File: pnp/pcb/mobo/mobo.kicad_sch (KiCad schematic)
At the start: 0 parts

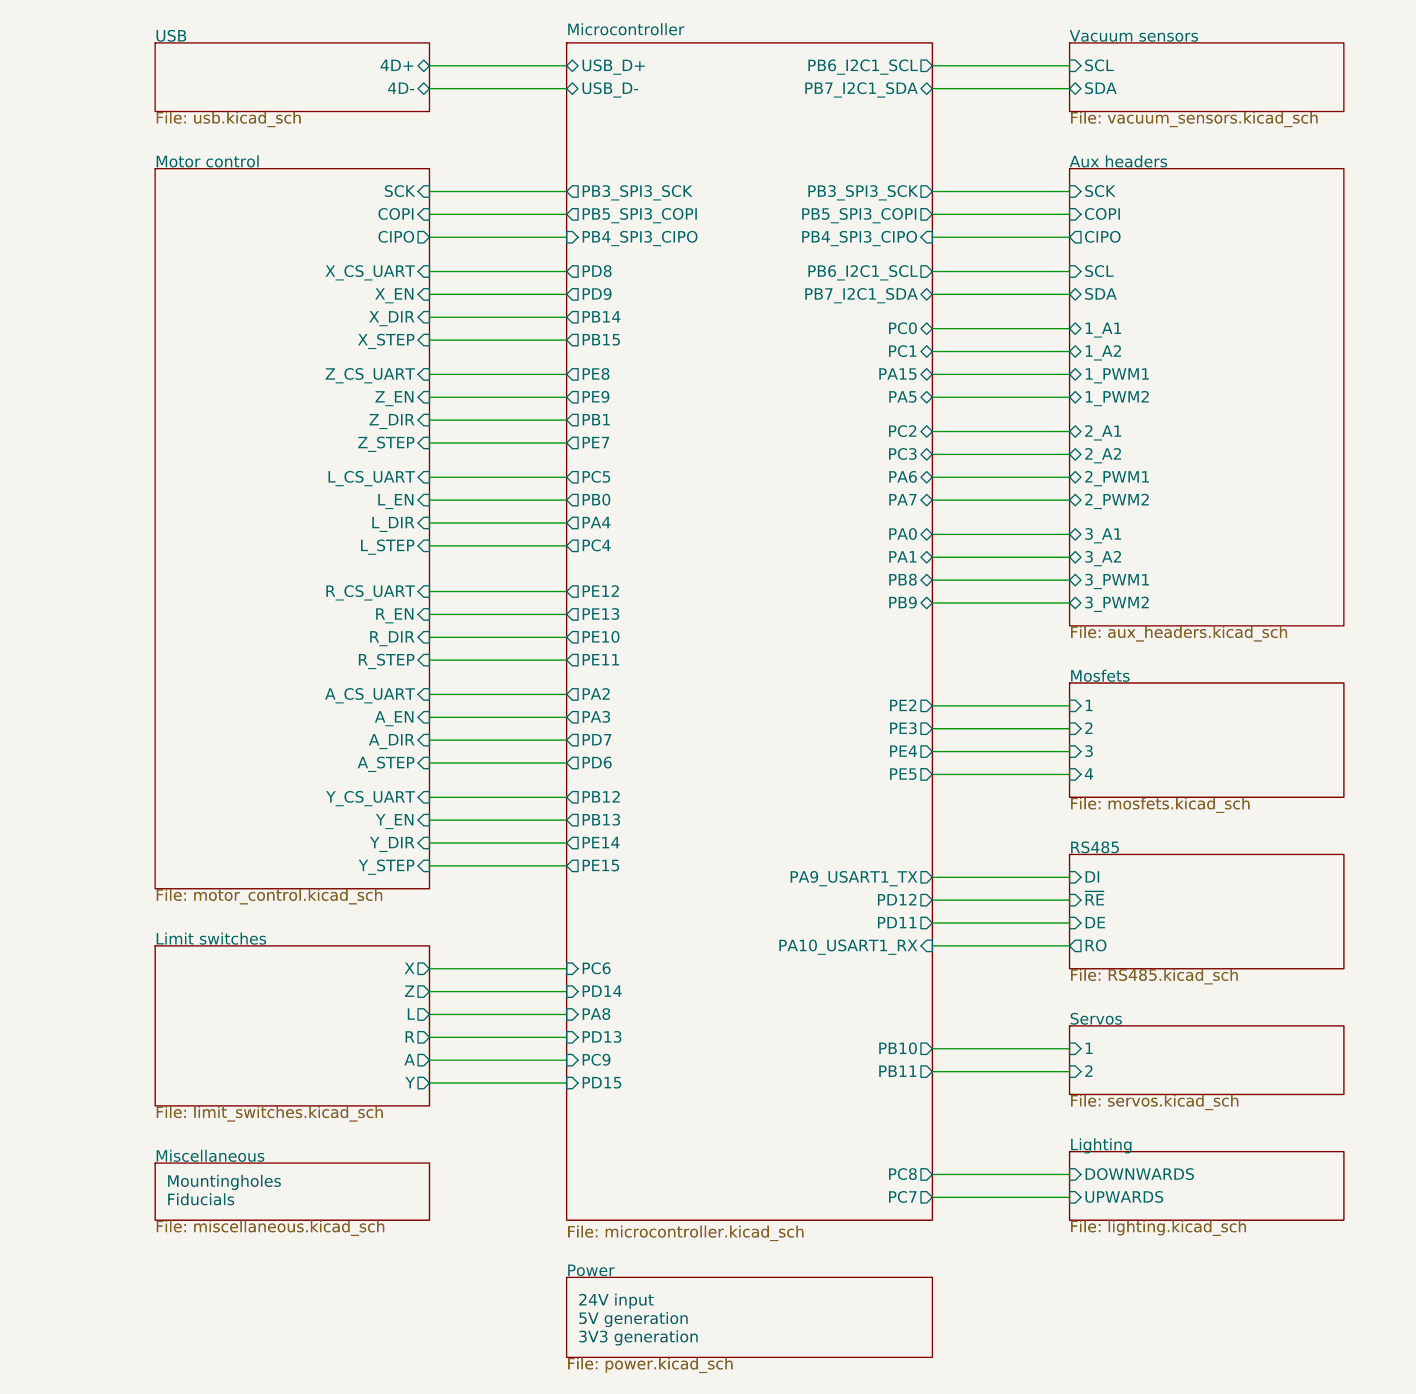
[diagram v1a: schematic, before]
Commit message: another huge chunk of work on rev04 of the mobo. breaks out diag and index pin for TMC2209 sensorless homing. reduces unique part count by consolidating resistor values where possible. replaces full ADC pipeline with monolithic I2C vacuum sensor and an I2C multiplexer due to address collision issues with two sensors. adds solder selectable jumpers for selecting whether an axis uses switch or TMC homing. redoes lots of routing of the SPI lines up to the stepper drivers.
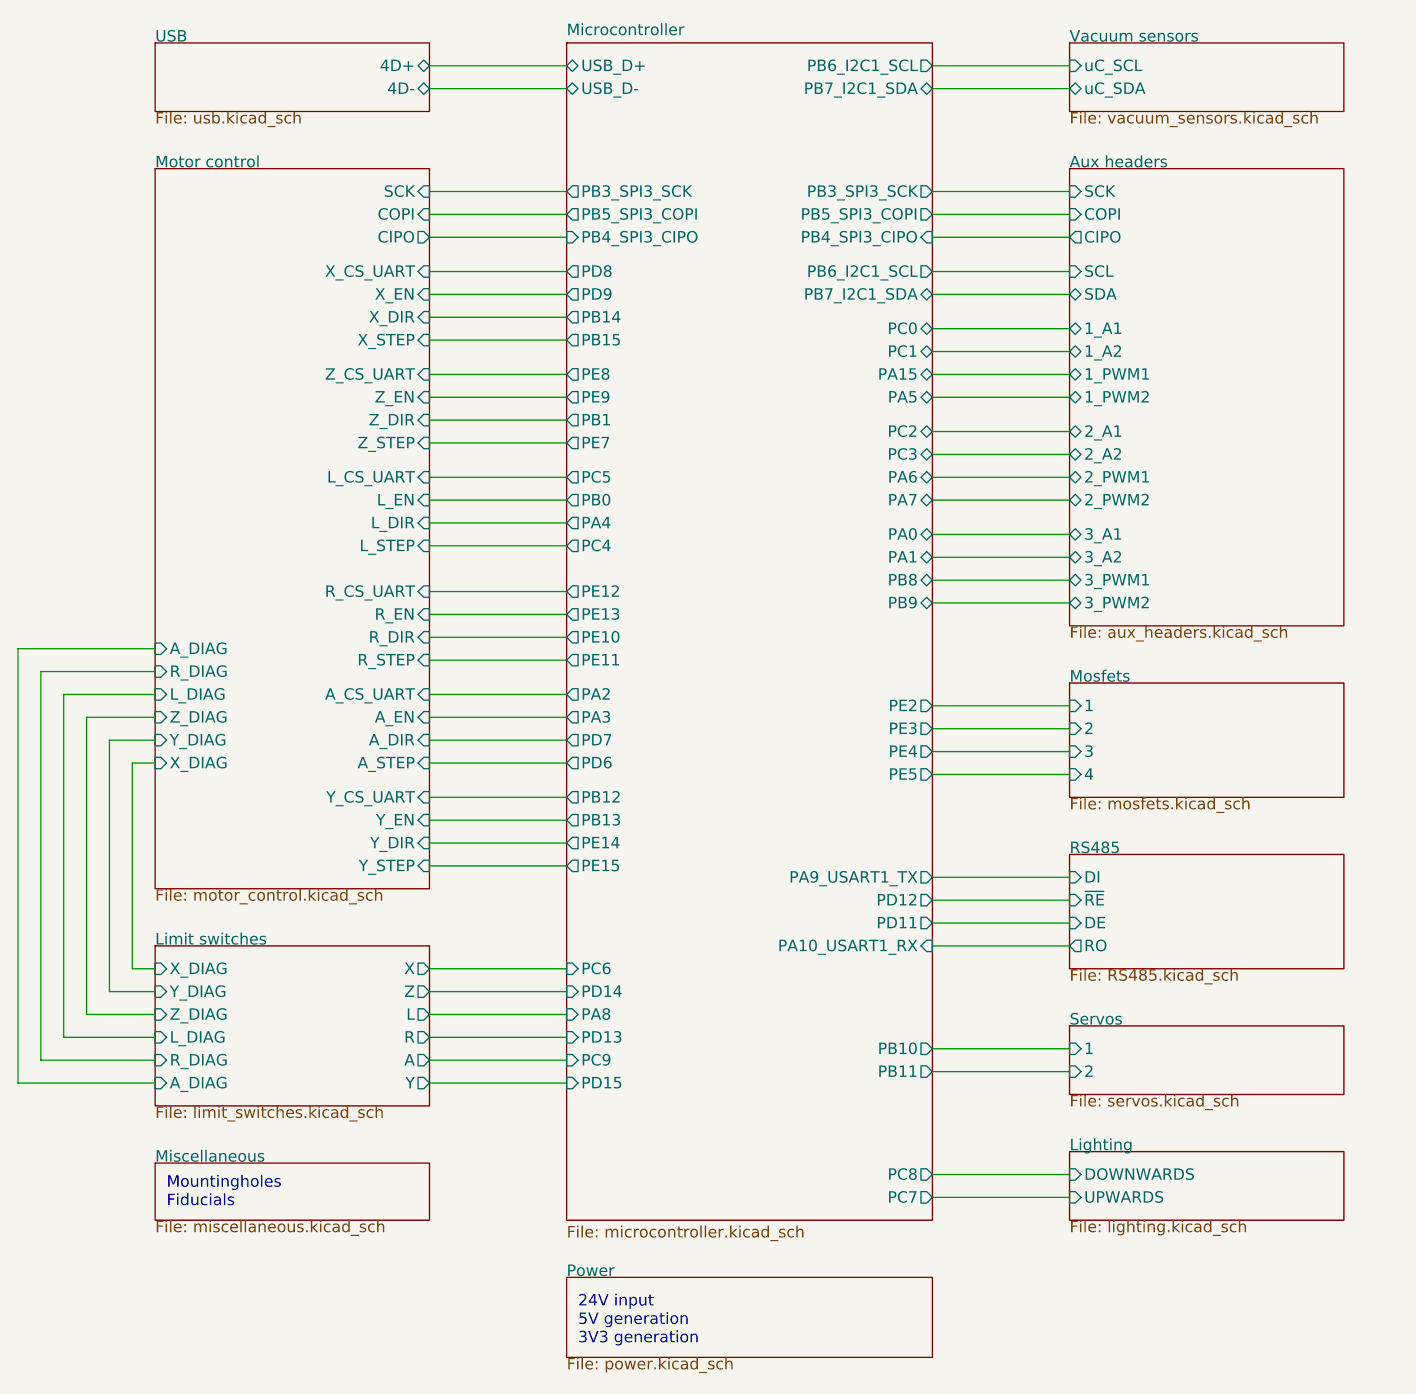
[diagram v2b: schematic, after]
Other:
- sheet Limit switches ports: added A_DIAG, L_DIAG, R_DIAG, X_DIAG, Y_DIAG, Z_DIAG; removed none
- sheet Motor control ports: added A_DIAG, L_DIAG, R_DIAG, X_DIAG, Y_DIAG, Z_DIAG; removed none
- sheet Vacuum sensors ports: added uC_SCL, uC_SDA; removed SCL, SDA
- company: (none) -> Opulo
- title: Index Mobo -> LumenPnP Motherboard
